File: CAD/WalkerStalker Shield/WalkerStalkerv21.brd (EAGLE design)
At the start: 49.5 x 53.3 mm, 25 parts

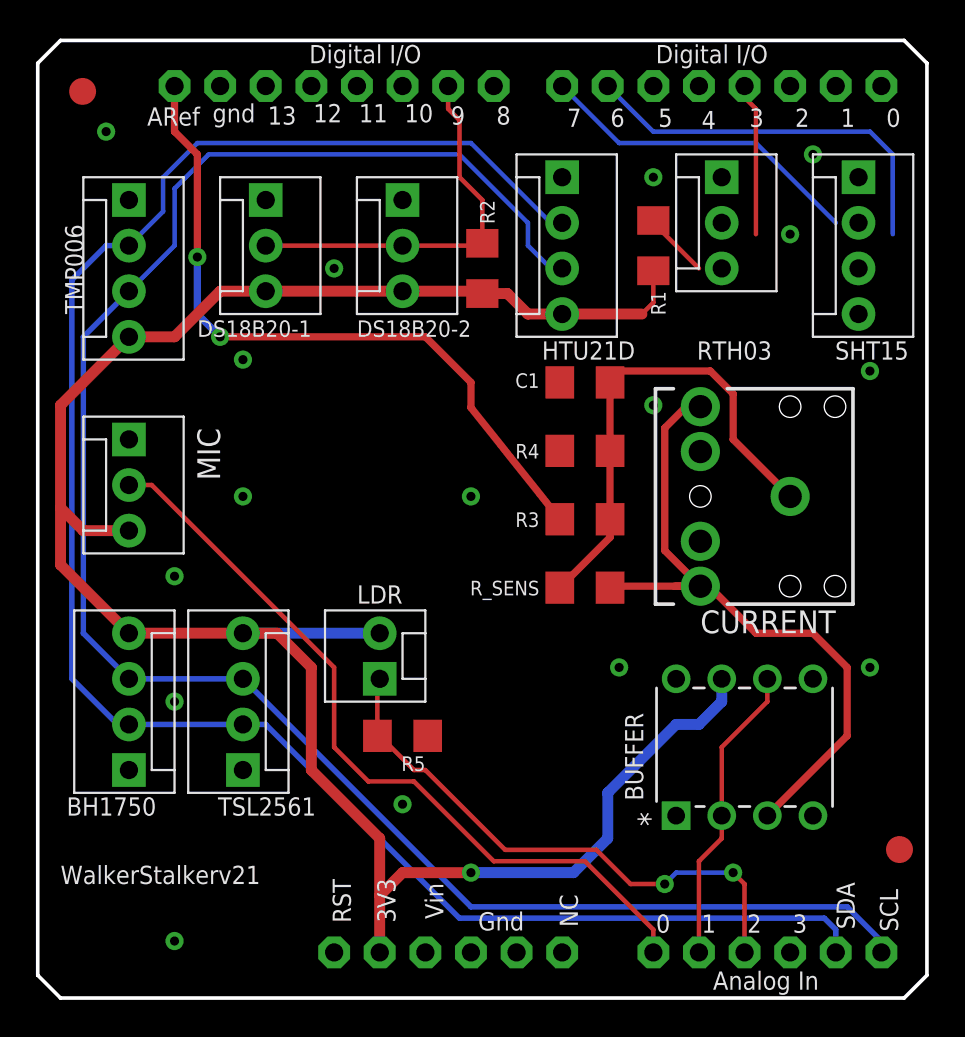
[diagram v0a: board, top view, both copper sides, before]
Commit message: Fixed Temperature sensors
+ Temperature sensors are now called by explicit address, rather than
index, which was not consistent (could not tell if sensor was wall or
air)
+ Unit IDs are not transmitted in data packets for easy identification
+Mounting bracket for TMP006 sensor added (3D file)
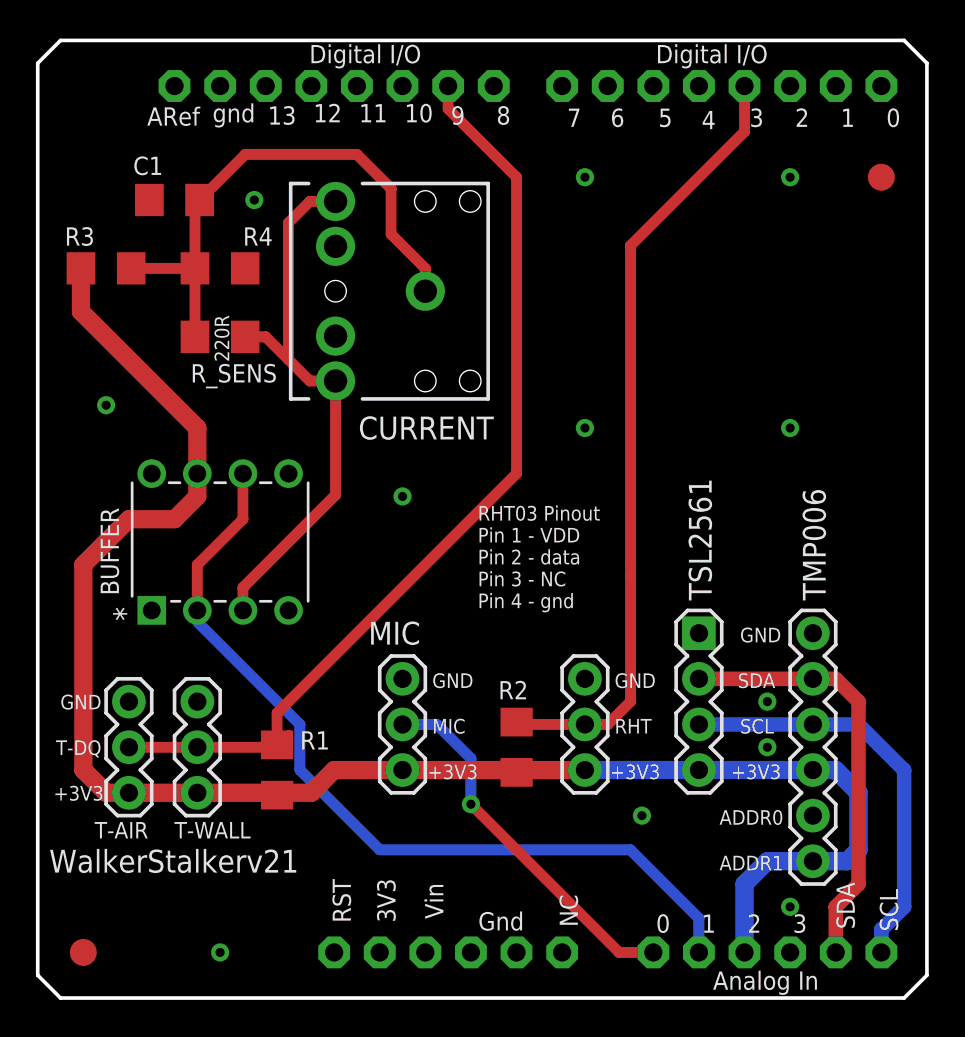
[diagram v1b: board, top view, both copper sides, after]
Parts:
- removed BH1: BH1750 BOB, SparkFun-Connectors:MOLEX-1X4
- removed DS18B20-1, DS18B20-2: DS18B20, SparkFun-Connectors:MOLEX-1X3
- removed HTU21D: HTU21D BOB, SparkFun-Connectors:MOLEX-1X4
- removed LDR: Mini Photocell, SparkFun-Connectors:MOLEX-1X2
- removed R5: 10K, SparkFun-Resistors:1206
- removed SHT1: SHT15 BOB, SparkFun-Connectors:MOLEX-1X4
- removed TMP1: TMP006 BOB, SparkFun-Connectors:MOLEX-1X4
- removed TSL1: TSL2561 BOB, SparkFun-Connectors:MOLEX-1X4
- added T-AIR, T-WALL: DS18B20, SparkFun-Connectors:1X03
- added TMP006: TMP006 BOB, SparkFun-Connectors:1X06
- added TSL2561: TSL2561 BOB, SparkFun-Connectors:1X04
- MIC: device SparkFun-Connectors:MOLEX-1X3 -> SparkFun-Connectors:1X03
- R1: value 10K -> 4.7K
- R3, R4: value 15K -> 22K
- RHT1: value RHT03 BOB -> RHT03; device SparkFun-Connectors:MOLEX-1X3 -> SparkFun-Connectors:1X03
- moved FID2 48.0 mm to (2.54, 2.54)
- moved FID1 37.5 mm to (47.0, 45.7)
- moved R1 36.0 mm to (13.3, 12.7)
- moved BUFFER 31.4 mm to (14.0, 29.2)
- moved R3 30.1 mm to (3.81, 40.6)
- moved RHT1 29.0 mm to (30.5, 17.8)
- moved R2 26.7 mm to (26.7, 14.0)
- moved C1 25.0 mm to (7.62, 44.5)
- moved R_SENS 24.7 mm to (10.2, 36.8)
- moved CURRENT 23.3 mm to (21.6, 39.4)
- moved R4 22.7 mm to (10.2, 40.6), turned to 180 degrees
- moved MIC 20.3 mm to (20.3, 17.8)
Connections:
- net D4 renamed TF-PWR
- net XBEE-PW renamed XBEE-PWR
- removed net LDR: JP-ANALOG.3, LDR.1, R5.2
- removed net SHT15-CL: JP-DIGITAL1.8, SHT1.3
- removed net SHT15-DA: JP-DIGITAL1.7, SHT1.2
- new net D6: JP-DIGITAL1.7
- new net D7: JP-DIGITAL1.8
- new net VCCIO: BUFFER.7, JP-ANALOG.3, MIC.3, R1.2, R2.2, R3.2, RHT1.3, T-AIR.3, T-WALL.3, TMP006.4, TMP006.6, TSL2561.4
- net +3V3: no longer BH1.4, BUFFER.7, DS18B20-1.3, DS18B20-2.3, HTU21D.4, LDR.2, MIC.3, R1.2, R2.2, RHT1.3, SHT1.4, TMP1.4, TSL1.4
- net AREF: no longer R3.2
- net GND: now also T-AIR.1, T-WALL.1, TMP006.1, TMP006.5, TSL2561.1; no longer BH1.1, DS18B20-1.1, DS18B20-2.1, HTU21D.1, R5.1, SHT1.1, TMP1.1, TSL1.1
- net RHT03: now also R2.1; no longer R1.1
- net SCL: now also TMP006.3, TSL2561.3; no longer BH1.3, HTU21D.3, TMP1.3, TSL1.3
- net SDA: now also TMP006.2, TSL2561.2; no longer BH1.2, HTU21D.2, TMP1.2, TSL1.2
- net TEMP_DQ: now also R1.1, T-AIR.2, T-WALL.2; no longer DS18B20-1.2, DS18B20-2.2, R2.1
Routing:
- net +3V3: track 119.1 -> 0.00 mm, vias 1 -> 0
- net VCCIO: track 0.00 -> 94.0 mm
- net SCL: track 104.8 -> 23.2 mm
- net SDA: track 105.2 -> 23.9 mm
- net AREF: track 39.4 -> 0.00 mm, vias 2 -> 0
- net RHT03: track 12.2 -> 43.9 mm
- net LDR: track 31.4 -> 0.00 mm, vias 2 -> 0
- net TEMP_DQ: track 21.7 -> 53.0 mm
- net I_SENS: track 16.8 -> 47.5 mm
- net MIC: track 43.3 -> 20.7 mm, vias 0 -> 1
- net SHT15-DA: track 21.9 -> 0.00 mm
- net SHT15-CL: track 18.4 -> 0.00 mm
- net N$1: track 38.9 -> 31.7 mm
- net N$2: track 27.3 -> 30.3 mm
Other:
- board text added: "+3V3"
- board text added: "220R"
- board text added: "ADDR0"
- board text added: "ADDR1"
- board text added: "GND"
- board text added: "MIC"
- board text added: "RHT"
- board text added: "RHT03 Pinout Pin 1 - VDD Pin 2 - data Pin 3 - NC Pin 4 - gnd"
- board text added: "T-DQ"
- board text removed: "BH1750"
- board text removed: "HTU21D"
- board text removed: "LDR"
- board text removed: "RTH03"
- board text removed: "SHT15"
- board text removed: "TMP006"
- board text removed: "TSL2561"
